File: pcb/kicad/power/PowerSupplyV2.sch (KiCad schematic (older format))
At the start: 35 parts, among them J1 12VWallWartVin, J2 OpAmpVsupply, J3 BackUpPower, J5 ResistorPinTest, J6 VSupplyLCDDisplay, J7 Vout1, J8 Vout2, J9 Vout3, U2 LM317H, U3 LM2574

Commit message: Add power supply to tile
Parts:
- removed 10u1: C, Capacitors_SMD:C_0603_HandSoldering, symbol C
- removed C5, C7: 1u, Capacitors_SMD:C_0805, symbol C
- removed C6, C9: 0.1u, Capacitors_SMD:C_0603_HandSoldering, symbol C
- removed D5: 11DQ05, Diodes_SMD:D_SOD-123, symbol D_Schottky_Small_ALT
- removed J5: ResistorPinTest, Pin_Headers:Pin_Header_Straight_1x02_Pitch2.54mm, symbol Screw_Terminal_1x02
- removed J6: VSupplyLCDDisplay, Pin_Headers:Pin_Header_Straight_1x02_Pitch2.54mm, symbol Screw_Terminal_1x02
- removed J7: Vout1, Pin_Headers:Pin_Header_Straight_1x02_Pitch2.54mm, symbol Screw_Terminal_1x02
- removed J9: Vout3, Pin_Headers:Pin_Header_Straight_1x02_Pitch2.54mm, symbol Screw_Terminal_1x02
- removed JP1: Jumper, Pin_Headers:Pin_Header_Straight_1x02_Pitch2.54mm, symbol Jumper
- removed U2: LM317H, Power_Integrations:TO-220, symbol LM317H
- added J4: Display, Pin_Headers:Pin_Header_Straight_1x02_Pitch2.54mm, symbol Screw_Terminal_1x02
- added R4: 120, Resistors_THT:R_Axial_DIN0309_L9.0mm_D3.2mm_P2.54mm_Vertical, symbol R
- C1, C2: footprint Capacitors_SMD:C_0805_HandSoldering -> Resistors_THT:R_Axial_DIN0204_L3.6mm_D1.6mm_P7.62mm_Horizontal
- C10, C3, C4: footprint Capacitors_SMD:C_0603_HandSoldering -> Resistors_THT:R_Axial_DIN0204_L3.6mm_D1.6mm_P7.62mm_Horizontal
- C8: footprint Capacitors_SMD:C_0805 -> Resistors_THT:R_Axial_DIN0204_L3.6mm_D1.6mm_P7.62mm_Horizontal
- D1: footprint LEDs:LED_0805 -> LEDs:LED_D5.0mm_Horizontal_O1.27mm_Z3.0mm
- D2, D3, D4, D6: footprint Diodes_SMD:D_SOD-123 -> Diodes_THT:D_DO-15_P15.24mm_Horizontal
- J8: value Vout2 -> Ucontroller
- L1: footprint Choke_SMD:Choke_SMD_10.4x10.4_H4.8 -> Inductors:SELF-WE-TPC_M
- R1, R2: footprint Resistors_SMD:R_0603_HandSoldering -> Resistors_THT:R_Axial_DIN0309_L9.0mm_D3.2mm_P2.54mm_Vertical
- R3: value 220 -> 160; footprint Resistors_SMD:R_0603_HandSoldering -> Resistors_THT:R_Axial_DIN0309_L9.0mm_D3.2mm_P2.54mm_Vertical
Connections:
- net labels added: 12Voutput, 5Voutput, PowerSupplyBase2.0
- net labels removed: AdjustTo4V
- wire segments 67 -> 47
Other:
- moved on the sheet: 220u1, 22u1, C1, C10, C3, C8, D1, D2, D3, D4, D6, F1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

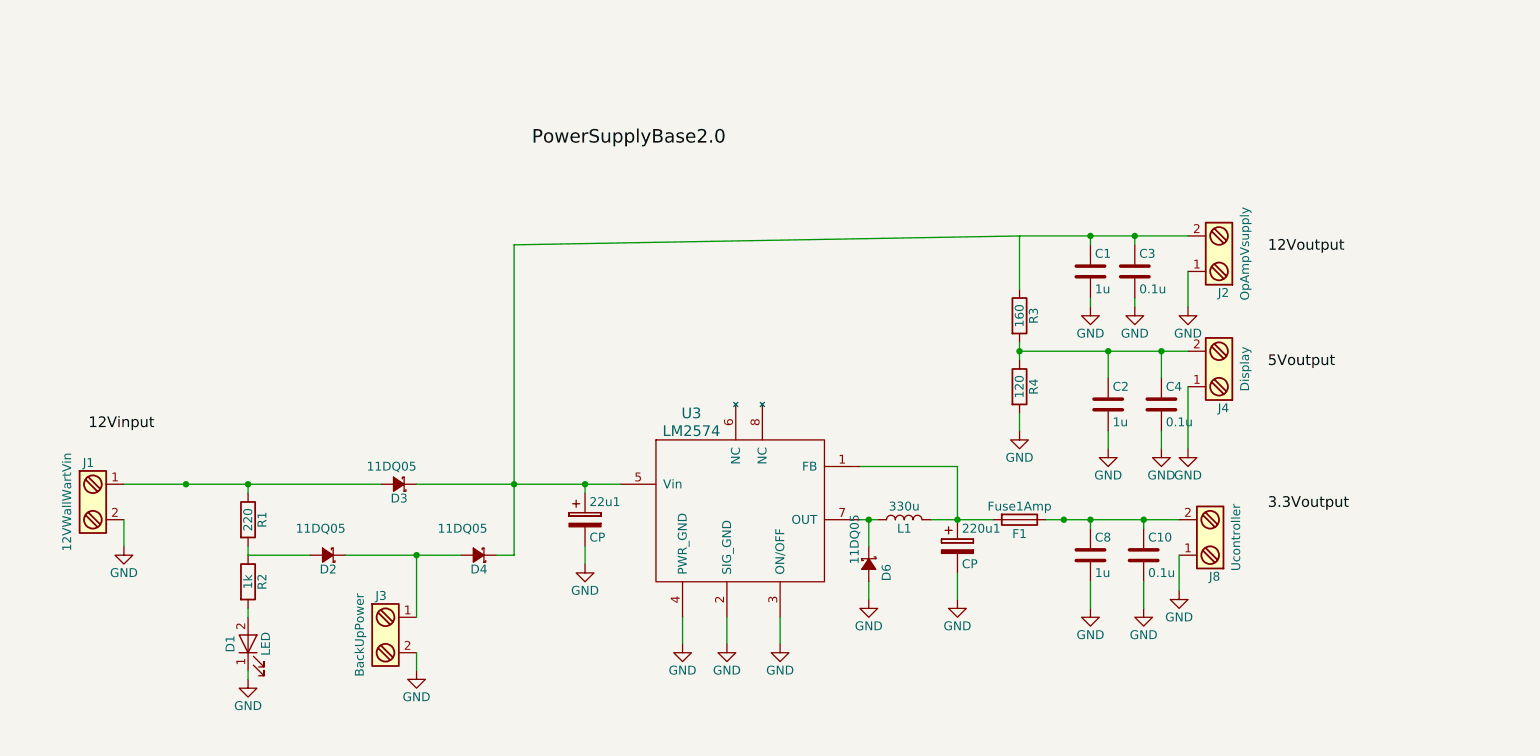
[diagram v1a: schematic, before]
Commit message: Tile uC and antenna boards
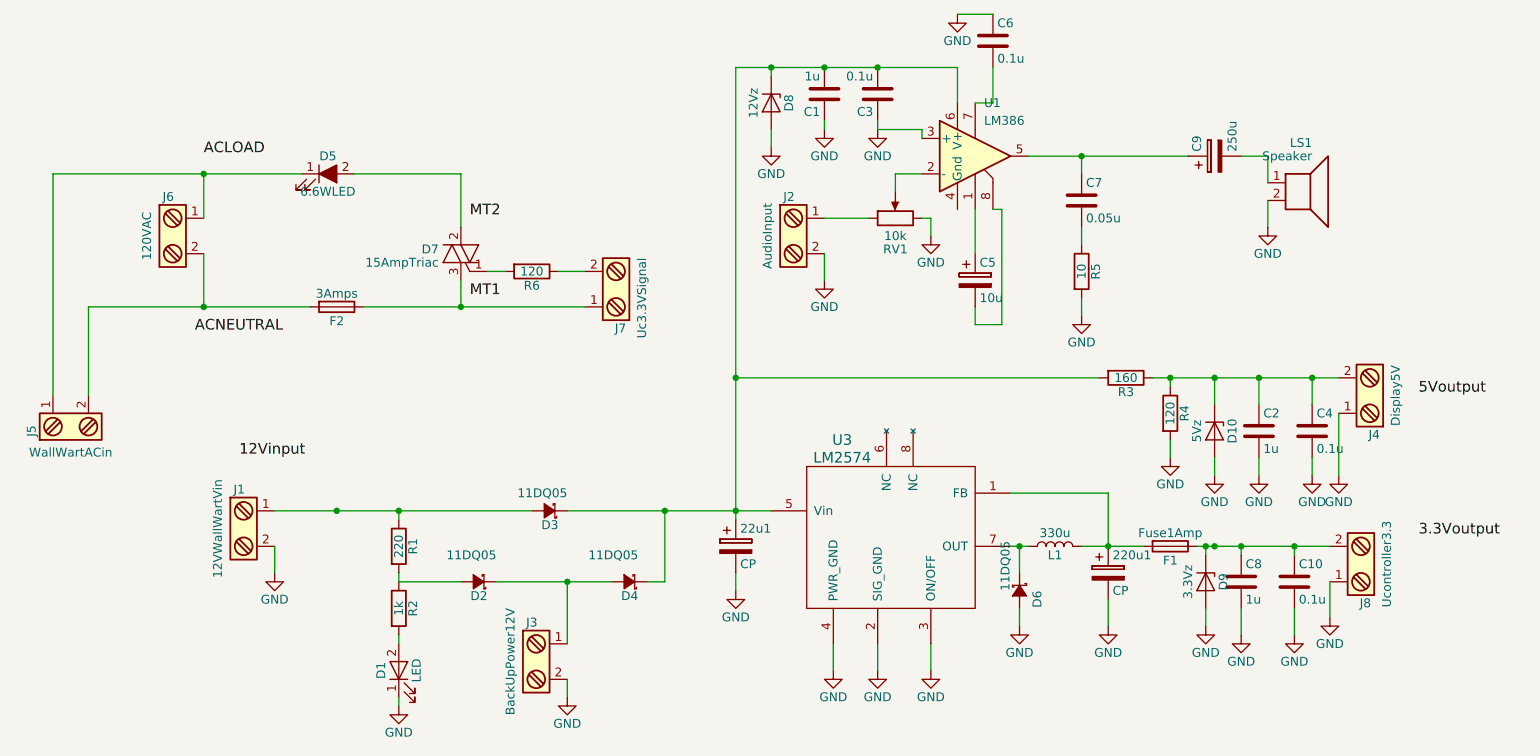
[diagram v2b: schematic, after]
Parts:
- added C5: 10u, Capacitors_THT:CP_Radial_D6.3mm_P2.50mm, symbol CP
- added C6: 0.1u, Resistors_THT:R_Axial_DIN0204_L3.6mm_D1.6mm_P7.62mm_Horizontal, symbol C
- added C7: 0.05u, Capacitors_SMD:C_0805_HandSoldering, symbol C
- added C9: 250u, Capacitors_THT:CP_Radial_D6.3mm_P2.50mm, symbol CP
- added D10: 5Vz, Diodes_SMD:D_SOT-23_ANK, symbol D_Zener
- added D5: 6.6WLED, Resistors_THT:R_Axial_DIN0204_L3.6mm_D1.6mm_P5.08mm_Horizontal, symbol LED_ALT
- added D7: 15AmpTriac, TO_SOT_Packages_THT:TO-220_Vertical, symbol Q_TRIAC_GAA
- added D8: 12Vz, Diodes_SMD:D_SOD-323_HandSoldering, symbol D_Zener
- added D9: 3.3Vz, Diodes_SMD:D_SOD-323_HandSoldering, symbol D_Zener
- added F2: 3Amps, Pin_Headers:Pin_Header_Straight_1x02_Pitch2.54mm, symbol Fuse
- added J5: WallWartACin, Resistors_THT:R_Axial_DIN0204_L3.6mm_D1.6mm_P5.08mm_Horizontal, symbol Screw_Terminal_1x02
- added J6: 120VAC, Resistors_THT:R_Axial_DIN0204_L3.6mm_D1.6mm_P5.08mm_Horizontal, symbol Screw_Terminal_1x02
- added J7: Uc3.3VSignal, Resistors_THT:R_Axial_DIN0204_L3.6mm_D1.6mm_P5.08mm_Horizontal, symbol Screw_Terminal_1x02
- added LS1: Speaker, Resistors_THT:R_Axial_DIN0204_L3.6mm_D1.6mm_P5.08mm_Horizontal, symbol Speaker
- added R5: 10, Resistors_SMD:R_0805_HandSoldering, symbol R
- added R6: 120, Resistors_SMD:R_0805_HandSoldering, symbol R
- added RV1: 10k, Potentiometers:Potentiometer_Alps_RK09K_Vertical, symbol POT
- added U1: LM386, Housings_DIP:DIP-8_W7.62mm, symbol LM386
- 22u1: footprint Capacitors_THT:CP_Radial_D10.0mm_P5.00mm -> Capacitors_THT:CP_Radial_D6.3mm_P2.50mm
- J1: footprint Pin_Headers:Pin_Header_Straight_1x02_Pitch2.54mm -> Connectors:BARREL_JACK
- J2: value OpAmpVsupply -> AudioInput; footprint Pin_Headers:Pin_Header_Straight_1x02_Pitch2.54mm -> Resistors_THT:R_Axial_DIN0204_L3.6mm_D1.6mm_P5.08mm_Horizontal
- J3: value BackUpPower -> BackUpPower12V; footprint Pin_Headers:Pin_Header_Straight_1x02_Pitch2.54mm -> Resistors_THT:R_Axial_DIN0204_L3.6mm_D1.6mm_P5.08mm_Horizontal
- J4: value Display -> Display5V; footprint Pin_Headers:Pin_Header_Straight_1x02_Pitch2.54mm -> Resistors_THT:R_Axial_DIN0204_L3.6mm_D1.6mm_P5.08mm_Horizontal
- J8: value Ucontroller -> Ucontroller3.3; footprint Pin_Headers:Pin_Header_Straight_1x02_Pitch2.54mm -> Resistors_THT:R_Axial_DIN0204_L3.6mm_D1.6mm_P5.08mm_Horizontal
- L1: footprint Inductors:SELF-WE-TPC_M -> Choke_SMD:Choke_SMD_7.3x7.3_H3.5
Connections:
- net GND: now also C1.1, C3.1, J2.2, C6.1, D10.2 (A), D8.2 (A), D9.2 (A), LS1.2, R5.2, RV1.3, U1.3 (+); no longer C1.2, C3.2, J2.1
- net at 22u1.1, D3.1 (K), D4.1 (K)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: now also C1.2, C3.2, R3.2, D8.1 (K), U1.6 (V+); no longer C1.1, C3.1, J2.2, R3.1
- net at C10.1, C8.1, F1.1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: now also D9.1 (K)
- net at C2.1, C4.1, J4.2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: now also R3.1, D10.1 (K); no longer R3.2
- new net: C5.1, U1.1
- new net: RV1.2, U1.2 (-)
- new net: C7.1, C9.1, U1.5
- new net: C6.2, U1.7
- new net: C5.2, U1.8
- new net: J2.1, RV1.1
- new net: C7.2, R5.1
- new net: C9.2, LS1.1
- new net: J7.2, R6.1
- new net: D7.1 (G), R6.2
- new net: D5.2 (A), D7.2 (A1)
- new net: D7.3 (A2), F2.1, J7.1
- new net: F2.2, J5.2, J6.2
- new net: D5.1 (K), J5.1, J6.1
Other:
- moved on the sheet: 220u1, 22u1, C10, C2, C4, C8, D1, D2, D3, D4, D6, F1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

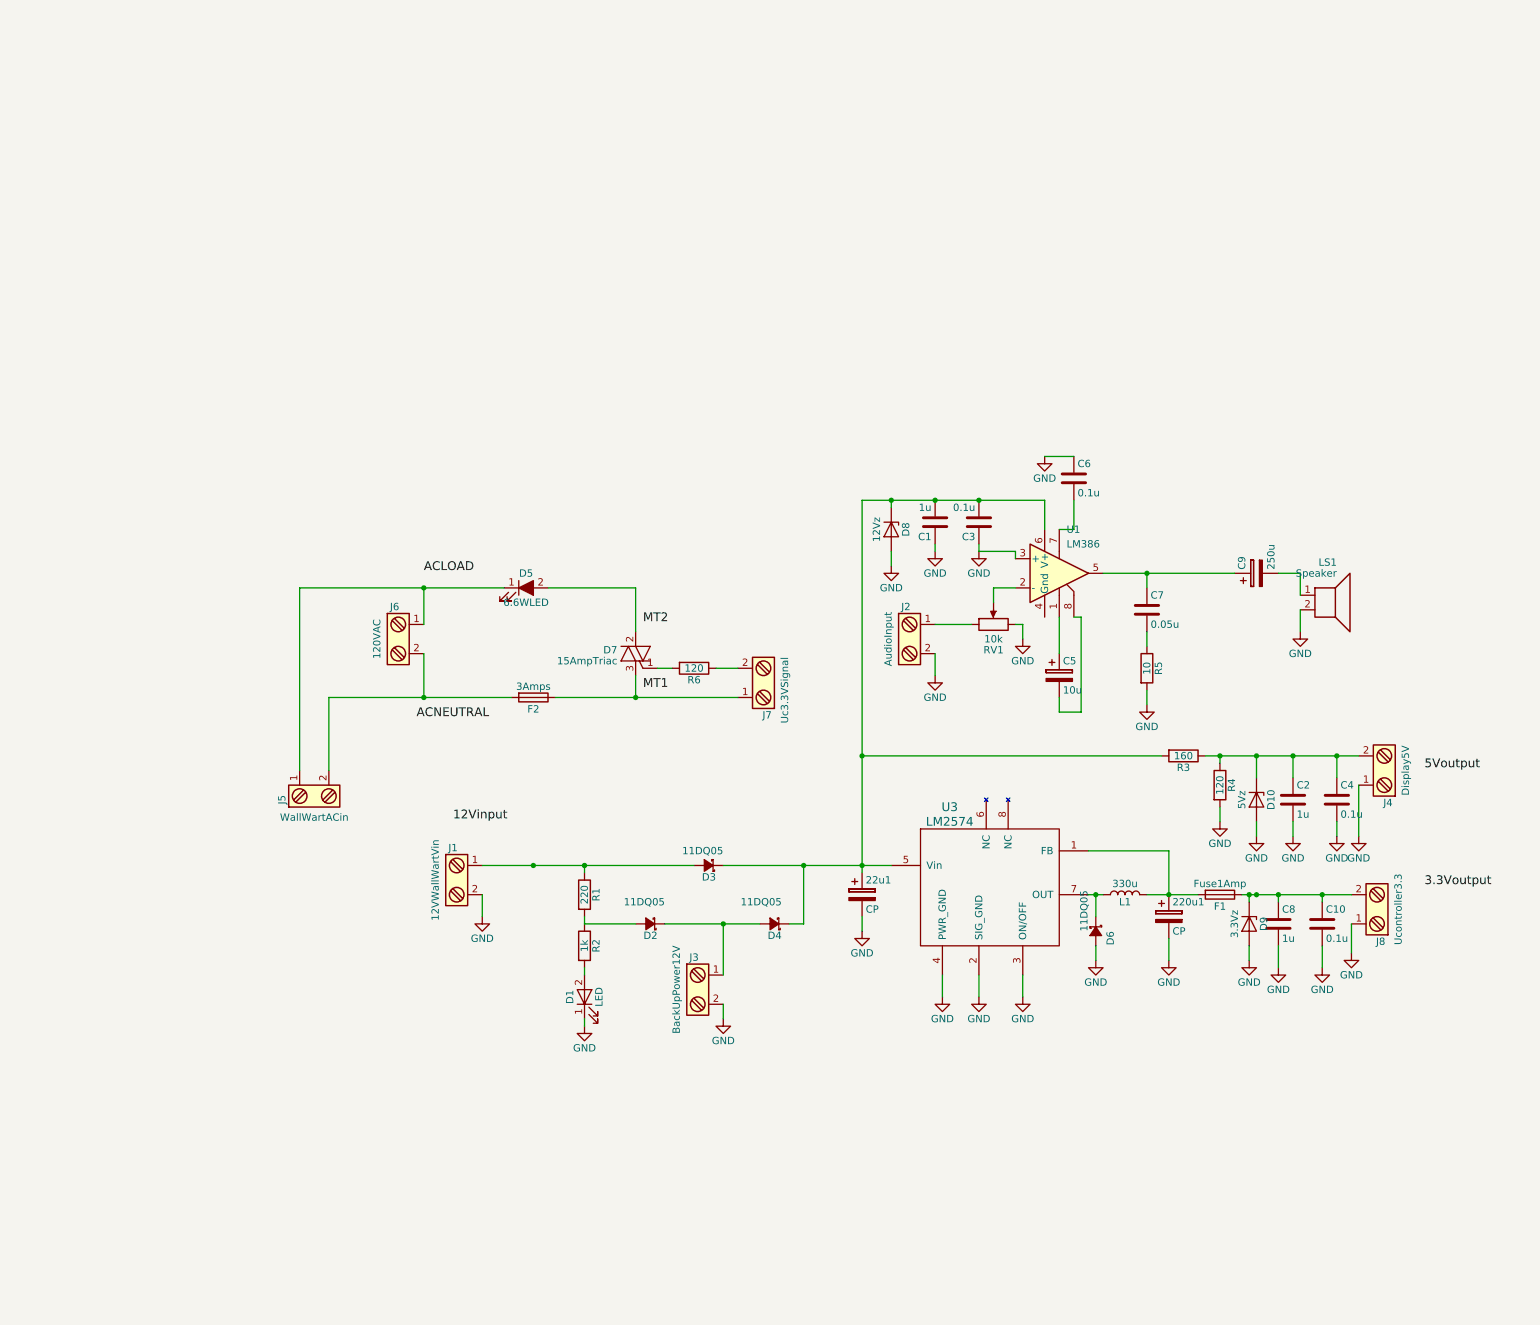
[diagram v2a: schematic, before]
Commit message: Finish new base station and tile boards
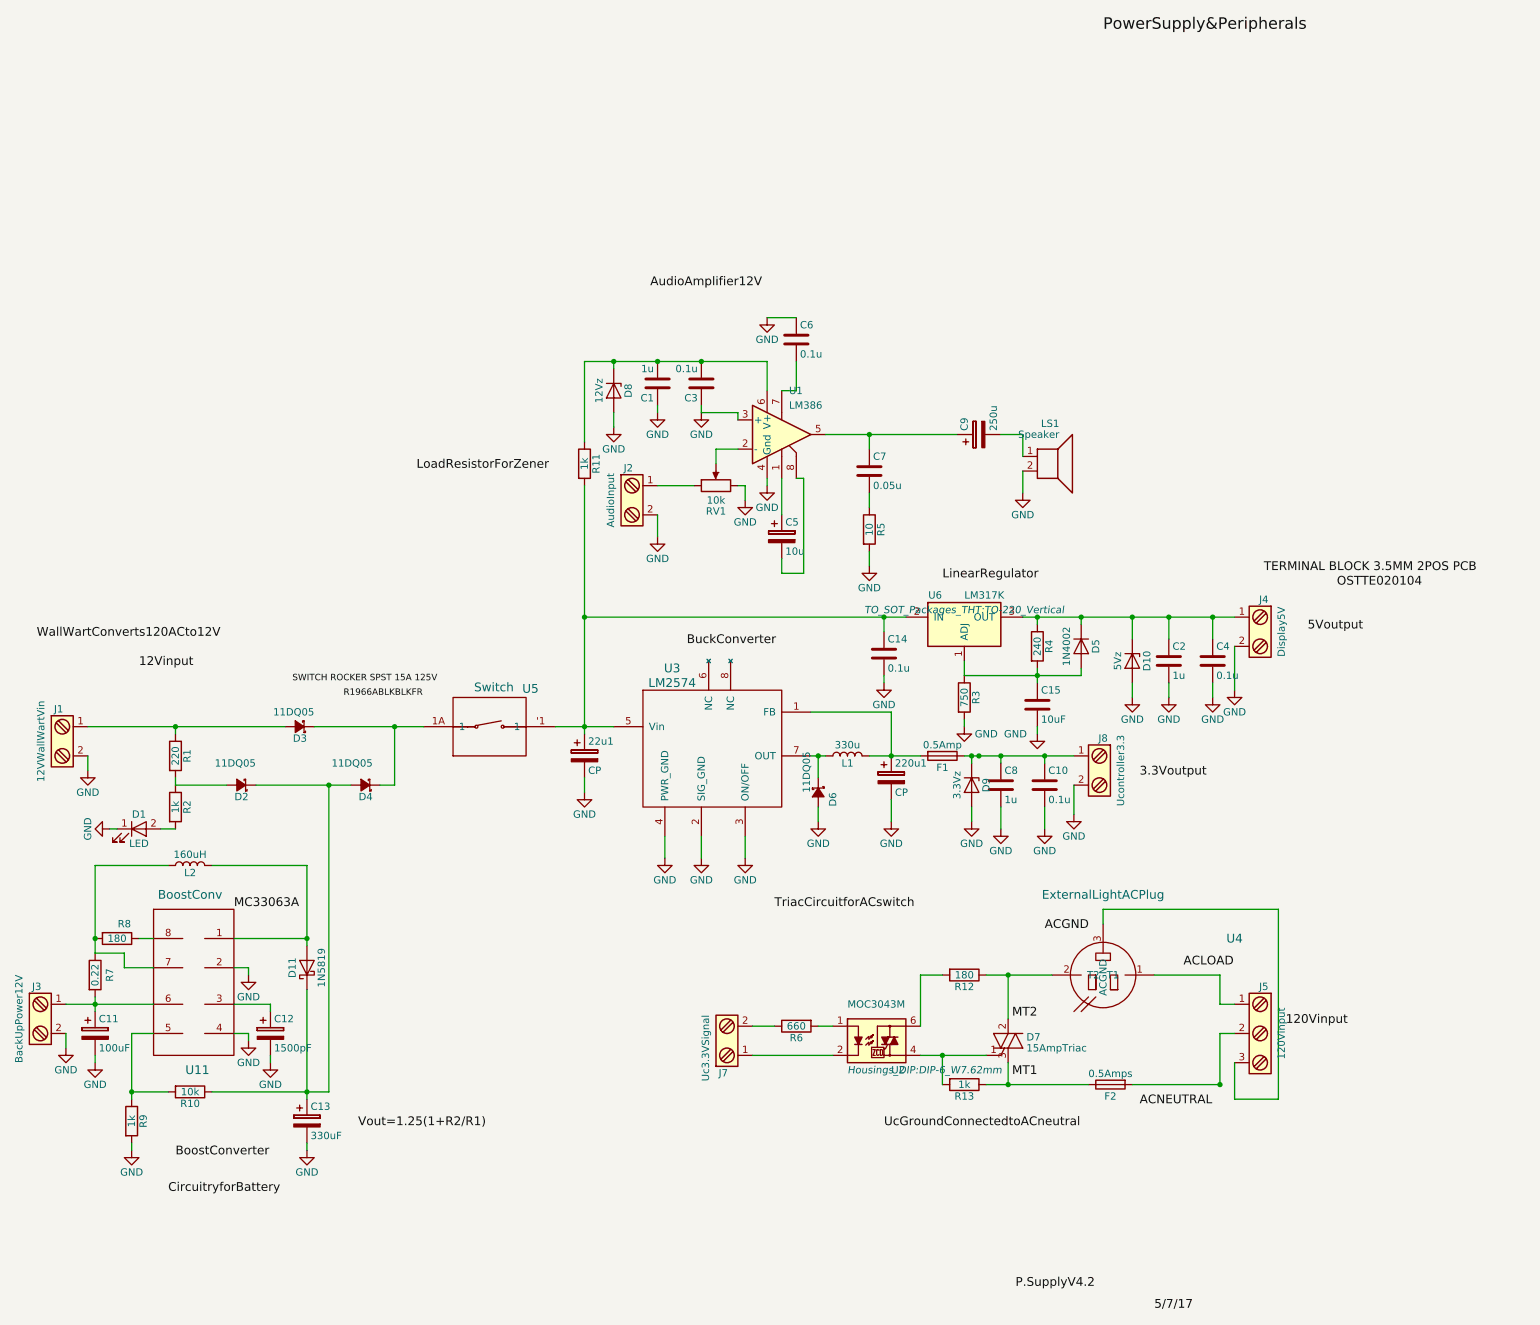
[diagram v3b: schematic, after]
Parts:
- removed D5: 6.6WLED, Resistors_THT:R_Axial_DIN0204_L3.6mm_D1.6mm_P5.08mm_Horizontal, symbol LED_ALT
- removed J5: WallWartACin, Resistors_THT:R_Axial_DIN0204_L3.6mm_D1.6mm_P5.08mm_Horizontal, symbol Screw_Terminal_1x02
- removed J6: 120VAC, Resistors_THT:R_Axial_DIN0204_L3.6mm_D1.6mm_P5.08mm_Horizontal, symbol Screw_Terminal_1x02
- added C11: 100uF, Capacitors_THT:CP_Radial_D6.3mm_P2.50mm, symbol CP
- added C12: 1500pF, Capacitors_THT:CP_Radial_D6.3mm_P2.50mm, symbol CP
- added C13: 330uF, Capacitors_THT:CP_Radial_D6.3mm_P2.50mm, symbol CP
- added C14: 0.1u, Resistors_THT:R_Axial_DIN0204_L3.6mm_D1.6mm_P7.62mm_Horizontal, symbol C
- added C15: 10uF, Resistors_THT:R_Axial_DIN0204_L3.6mm_D1.6mm_P7.62mm_Horizontal, symbol C
- added D11: 1N5819, Diodes_THT:D_DO-15_P5.08mm_Vertical_KathodeUp, symbol D_Schottky
- added D5: 1N4002, Diodes_THT:D_DO-15_P5.08mm_Vertical_KathodeUp, symbol D
- added J5: 120Vinput, Footprints:703w0053, symbol Screw_Terminal_1x03
- added L2: 160uH, Choke_SMD:Choke_SMD_12x12mm_h4.5mm, symbol L
- added R10: 10k, Resistors_THT:R_Axial_DIN0309_L9.0mm_D3.2mm_P2.54mm_Vertical, symbol R
- added R11, R13, R9: 1k, Resistors_THT:R_Axial_DIN0309_L9.0mm_D3.2mm_P2.54mm_Vertical, symbol R
- added R12, R8: 180, Resistors_THT:R_Axial_DIN0309_L9.0mm_D3.2mm_P2.54mm_Vertical, symbol R
- added R7: 0.22, Resistors_THT:R_Axial_DIN0309_L9.0mm_D3.2mm_P2.54mm_Vertical, symbol R
- added U11: BoostConv, Housings_DIP:DIP-8_W7.62mm, symbol BoostConv
- added U2: MOC3043M, Housings_DIP:DIP-6_W7.62mm, symbol MOC3043M
- added U4: ExternalLightACPlug, Footprints:739W-X203, symbol ExternalLightACPlug
- added U5: Switch, Footprints:Switch, symbol Switch
- added U6: LM317K, TO_SOT_Packages_THT:TO-220_Vertical, symbol LM317K
- D2, D3, D4, D6: footprint Diodes_THT:D_DO-15_P15.24mm_Horizontal -> Diodes_THT:D_DO-15_P5.08mm_Vertical_KathodeUp
- F1: value Fuse1Amp -> 0.5Amp; footprint Pin_Headers:Pin_Header_Straight_1x02_Pitch2.54mm -> Footprints:FuseTH500mA
- F2: value 3Amps -> 0.5Amps; footprint Pin_Headers:Pin_Header_Straight_1x02_Pitch2.54mm -> Footprints:FuseTH500mA
- J2, J4, J7, J8, LS1: footprint Resistors_THT:R_Axial_DIN0204_L3.6mm_D1.6mm_P5.08mm_Horizontal -> Footprints:BlockTerminal3.5mm
- J3: footprint Resistors_THT:R_Axial_DIN0204_L3.6mm_D1.6mm_P5.08mm_Horizontal -> Footprints:NIMH4.8V
- L1: footprint Choke_SMD:Choke_SMD_7.3x7.3_H3.5 -> Choke_SMD:Choke_SMD_12x12mm_h4.5mm
- R3: value 160 -> 750
- R4: value 120 -> 240
- R6: value 120 -> 660; footprint Resistors_SMD:R_0805_HandSoldering -> Resistors_THT:R_Axial_DIN0309_L9.0mm_D3.2mm_P2.54mm_Vertical
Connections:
- net GND: now also J4.2, J8.2, R3.2, U1.4 (Gnd), C11.2, C12.2, C13.2, C14.2, C15.2, R9.2, U11.2, U11.4; no longer J4.1, J8.1, R4.2
- net at C10.1, C8.1, D9.1 (K)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: now also J8.1; no longer J8.2
- net at D2.1 (K), D4.2 (A): now also C13.1, D11.1 (K), R10.1; no longer J3.1
- net at C2.1, C4.1, D10.1 (K)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: now also J4.1, D5.1 (K), U6.3 (OUT); no longer J4.2, R3.1
- net at R6.2: now also U2.1; no longer D7.1 (G)
- net at D7.2 (A1): now also R12.1, U4.2 (T2)
- net at D7.3 (A2), F2.1: now also R13.1; no longer J7.1
- net at F2.2: now also J5.2
- new net: 22u1.1, C14.1, R11.2, U3.5 (Vin), U5.'1 (1), U6.2 (IN)
- new net: D3.1 (K), D4.1 (K), U5.1A (1)
- new net: C11.1, J3.1, R7.2, U11.6
- new net: C1.2, C3.2, D8.1 (K), R11.1, U1.6 (V+)
- new net: D7.1 (G), R13.2, U2.4
- new net: J7.1, U2.2
- new net: D11.2 (A), L2.2, U11.1
- new net: C12.1, U11.3
- new net: R10.2, R9.1, U11.5
- new net: L2.1, R7.1, R8.2, U11.7
- new net: R8.1, U11.8
- new net: R12.2, U2.6
- new net: J5.1, U4.1 (T1)
- new net: J5.3, U4.3 (ACGND)
- new net: C15.1, D5.2 (A), R3.1, R4.2, U6.1 (ADJ)
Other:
- moved on the sheet: 220u1, 22u1, C1, C10, C2, C3, C4, C5, C6, C7, C8, C9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

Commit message: Add power supply to tile
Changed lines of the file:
@@
 	1    0    0    -1
 $EndComp
+Wire Wire Line
+	8900 3700 7950 3700
+Connection ~ 7950 3700
+Wire Wire Line
+	8450 3850 8450 3700
+Connection ~ 8450 3700
+Wire Wire Line
+	8750 3850 8750 3700
+Connection ~ 8750 3700
 $Comp
 L R R12
